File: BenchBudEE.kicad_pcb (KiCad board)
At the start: 2 copper layers, 0 parts

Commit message: Initial Relay PCB Layout
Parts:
- added D1: LG Q971-KN-1, LED-0603, F.Cu at (193.0, 73.7)
- added D2: B130-13-F, SMA, B.Cu at (207.0, 74.9)
- added K1: 1461069-5, TE-SPDT, F.Cu at (201.9, 72.4)
- added Q1: MMBT3904-7-F, SOT23EBC, B.Cu at (199.4, 76.2)
- added R1: 500, SM0805, F.Cu at (185.4, 74.9)
- added R2: 200, SM0805, B.Cu at (193.0, 77.5)
- added R3: 0, SM0805, F.Cu at (198.1, 67.3)
- added R4: 100, SM0805, B.Cu at (199.4, 69.8)
- added R5: 0, SM0805, B.Cu at (207.0, 67.3)
- added R6: 0, SM0805, B.Cu at (205.7, 78.7)
- added U1: LTV-816S, 4-SMD, F.Cu at (184.2, 69.8)
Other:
- board outline added: 165.1 x 63.5 mm
- copper layers 2 -> 4
- rule pad_to_mask_clearance: 0 -> 0.254
- rule trace_min: 0.254 -> 0.1524
- rule via_min_drill: 0.508 -> 0.3302
- rule via_min_size: 0.889 -> 0.508

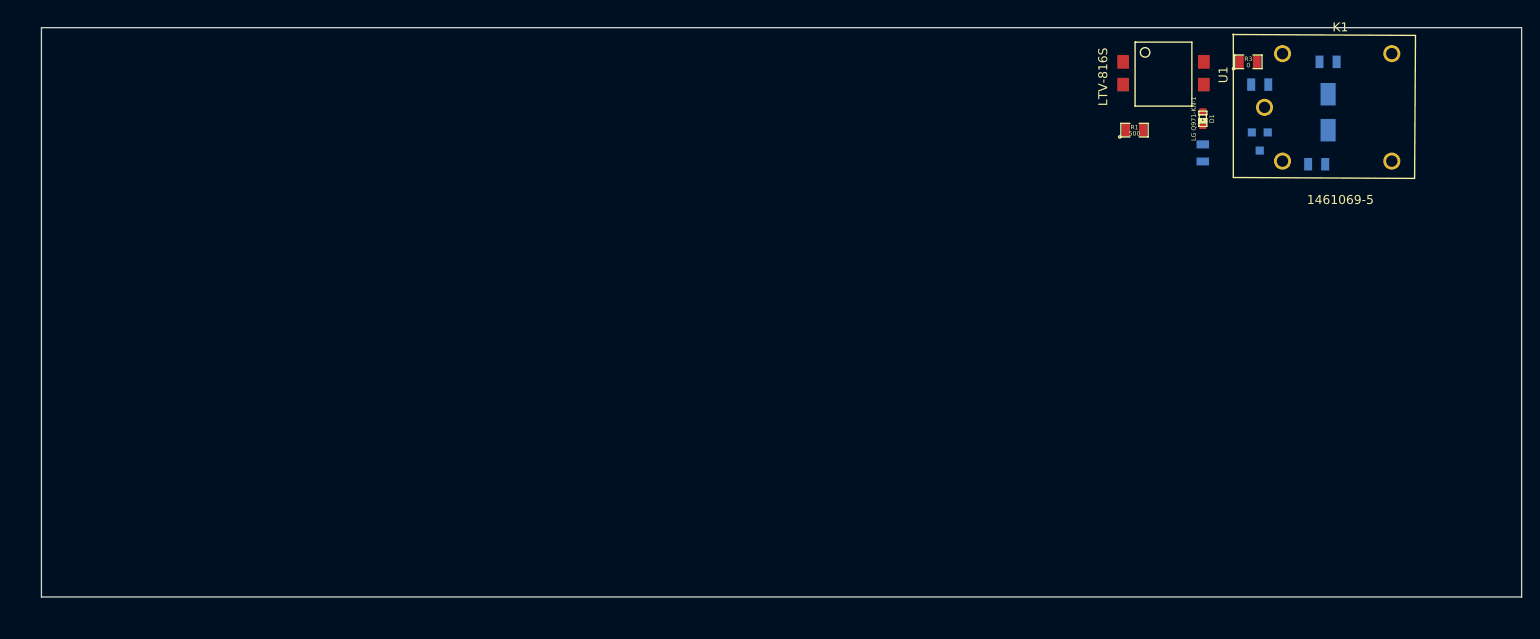
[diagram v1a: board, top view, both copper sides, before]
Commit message: Added Arduino Connect Pin Layout
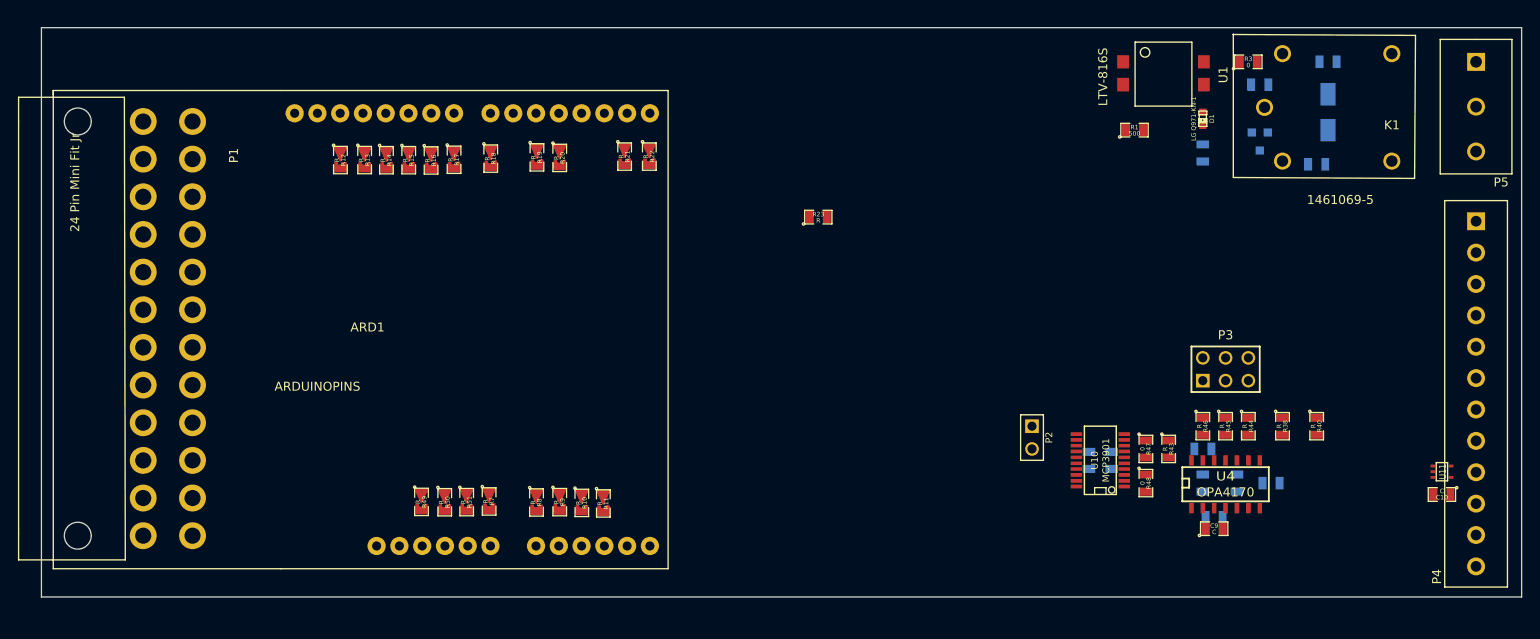
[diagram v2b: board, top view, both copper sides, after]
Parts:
- added ARD1: ARDUINOPINS, Arduino, F.Cu at (99.4, 99.0)
- added C10: C, SM0805, F.Cu at (219.7, 115.6)
- added C5: C, SM0805, B.Cu at (182.9, 111.8)
- added C6: C, SM0805, B.Cu at (180.3, 111.8)
- added C7: C, SM0805, B.Cu at (194.3, 118.1)
- added C8: C, SM0805, B.Cu at (193.0, 110.5)
- added C9: C, SM0805, F.Cu at (194.3, 119.4)
- added P1: 24 Pin Mini Fit Jr, ATX_Header, F.Cu at (74.9, 74.0)
- added P2: CONN_2, PIN_ARRAY_2X1, F.Cu at (174.0, 109.2)
- added P3: CONN_3X2, pin_array_3x2, F.Cu at (195.6, 101.6)
- added P4: 12 Pin Terminal Block, 12pinTB, F.Cu at (223.5, 85.1)
- added P5: 3 Pin TB, 3pinTB, F.Cu at (223.5, 67.3)
- added R10: R, SM0805-Blob, F.Cu at (123.8, 116.5)
- added R11: R, SM0805-Blob, F.Cu at (126.2, 116.6)
- added R12: R, SM0805-Blob, F.Cu at (96.8, 78.3)
- added R13: R, SM0805-Blob, F.Cu at (99.6, 78.3)
- added R14: R, SM0805-Blob, F.Cu at (102.0, 78.3)
- added R15: R, SM0805-Blob, F.Cu at (104.5, 78.3)
- added R16: R, SM0805-Blob, F.Cu at (107.0, 78.3)
- added R17: R, SM0805-Blob, F.Cu at (109.5, 78.2)
- added R18: R, SM0805-Blob, F.Cu at (113.6, 78.1)
- added R19: R, SM0805-Blob, F.Cu at (118.8, 78.0)
- added R20: R, SM0805-Blob, F.Cu at (121.3, 78.0)
- added R21: R, SM0805-Blob, F.Cu at (128.5, 77.9)
- added R22: R, SM0805-Blob, F.Cu at (131.3, 77.9)
- added R23: R, SM0805, F.Cu at (150.2, 84.6)
- added R38: R, SM0805, F.Cu at (201.9, 108.0)
- added R39: R, SM0805, B.Cu at (196.8, 114.3)
- added R40: R, SM0805, F.Cu at (205.7, 108.0)
- added R41: R, SM0805, B.Cu at (193.0, 114.3)
- added R42: R, SM0805, B.Cu at (200.7, 114.3)
- added R43: R, SM0805, F.Cu at (189.2, 110.5)
- added R44: R, SM0805, F.Cu at (198.1, 108.0)
- added R45: R, SM0805, F.Cu at (195.6, 108.0)
- added R46: R, SM0805, F.Cu at (193.0, 108.0)
- added R47: 0, SM0805, F.Cu at (186.7, 110.5)
- added R48: 0, SM0805, F.Cu at (186.7, 114.3)
- added R49: R, SM0805-Blob, F.Cu at (105.9, 116.4)
- added R50: R, SM0805-Blob, F.Cu at (108.5, 116.4)
- added R51: R, SM0805-Blob, F.Cu at (110.9, 116.4)
- added R7: R, SM0805-Blob, F.Cu at (113.4, 116.3)
- added R8: R, SM0805-Blob, F.Cu at (118.7, 116.5)
- added R9: R, SM0805-Blob, F.Cu at (121.3, 116.4)
- added U10: MCP3901, SSOP20, F.Cu at (181.6, 111.8)
- added U11: LMT84, SOT353, F.Cu at (219.7, 113.0)
- added U4: OPA4170, SO14E, F.Cu at (195.6, 114.3)
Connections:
- K1 pad 1: (no net) -> /Relay/RELAY_COM
- K1 pad 3: (no net) -> /Relay/RELAY_NO
- K1 pad 4: (no net) -> /Relay/RELAY_NC

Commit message: Associate and Place Power Component
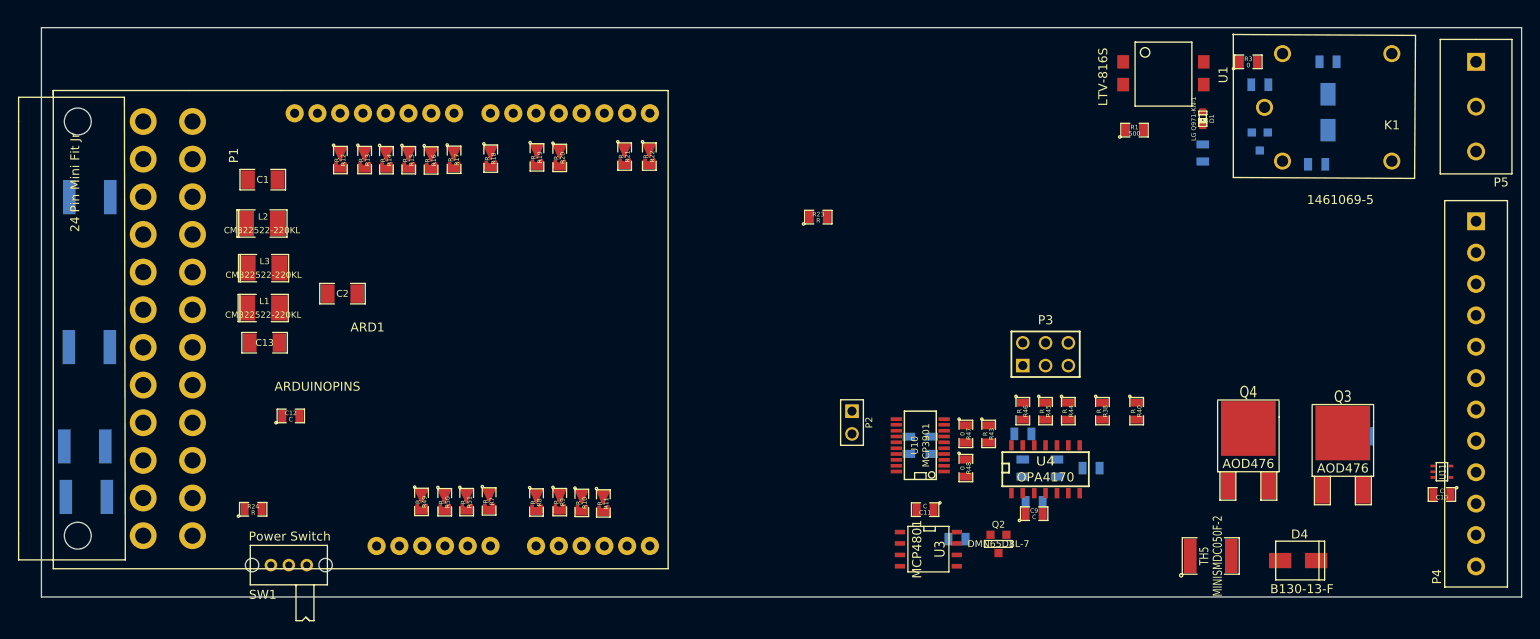
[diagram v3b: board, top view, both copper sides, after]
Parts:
- added C1: C, SM1206, F.Cu at (88.2, 80.5)
- added C11: C, SM0805, F.Cu at (162.1, 117.3)
- added C12: C, SM0805, F.Cu at (91.3, 106.8)
- added C13: C, SM1206, F.Cu at (88.4, 98.6)
- added C2: C, SM1206, F.Cu at (97.1, 93.2)
- added D4: B130-13-F, SMA, F.Cu at (201.7, 122.9)
- added L1: CM322522-220KL, SM1210L, F.Cu at (88.2, 94.8)
- added L2: CM322522-220KL, SM1210L, F.Cu at (88.1, 85.3)
- added L3: CM322522-220KL, SM1210L, F.Cu at (88.3, 90.3)
- added Q2: DMN65D8L-7, SOT23GDS, F.Cu at (170.2, 121.1)
- added Q3: AOD476, DPAK2, F.Cu at (208.7, 115.1)
- added Q4: AOD476, DPAK2, F.Cu at (198.1, 114.6)
- added R24: R, SM0805, F.Cu at (87.1, 117.2)
- added R26: R, SM0805, B.Cu at (165.6, 120.5)
- added R27: R, SM1206, B.Cu at (209.6, 109.1)
- added SW1: Power Switch, BB_switch, F.Cu at (87.0, 123.4)
- added TH1: MINISMDC050F-2, SM1812, B.Cu at (68.5, 115.8)
- added TH2: MINISMDC050F-2, SM1812, B.Cu at (68.8, 99.1)
- added TH3: MINISMDC050F-2, SM1812, B.Cu at (68.9, 82.4)
- added TH4: MINISMDC050F-2, SM1812, B.Cu at (68.3, 110.2)
- added TH5: MINISMDC050F-2, SM1812, F.Cu at (193.9, 122.4)
- added U3: MCP4801, SO8N, F.Cu at (162.4, 121.7)
- moved P3 20.1 mm to (175.5, 99.9)
- moved R45 20.1 mm to (175.5, 106.3)
- moved U10 20.1 mm to (161.5, 110.1)
- moved U4 20.1 mm to (175.5, 112.6)
- moved C5 20.1 mm to (162.8, 110.1)
- moved C6 20.1 mm to (160.3, 110.1)
- moved C7 20.1 mm to (174.2, 116.4)
- moved C8 20.1 mm to (173.0, 108.8)
- moved C9 20.1 mm to (174.2, 117.7)
- moved P2 20.1 mm to (153.9, 107.5)
- moved R38 20.1 mm to (181.9, 106.3)
- moved R39 20.1 mm to (176.8, 112.6)
- moved R40 20.1 mm to (185.7, 106.3)
- moved R41 20.1 mm to (173.0, 112.6)
- moved R42 20.1 mm to (180.6, 112.6)
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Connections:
- net /Arduino/ADC_CS_N renamed /Arduino/~ADC_CS
- ARD1 pad 13: (no net) -> N-0000050
- ARD1 pad 14: (no net) -> N-0000049
